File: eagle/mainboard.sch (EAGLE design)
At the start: 8 parts, among them Q1 TIP122, Q2 TIP122

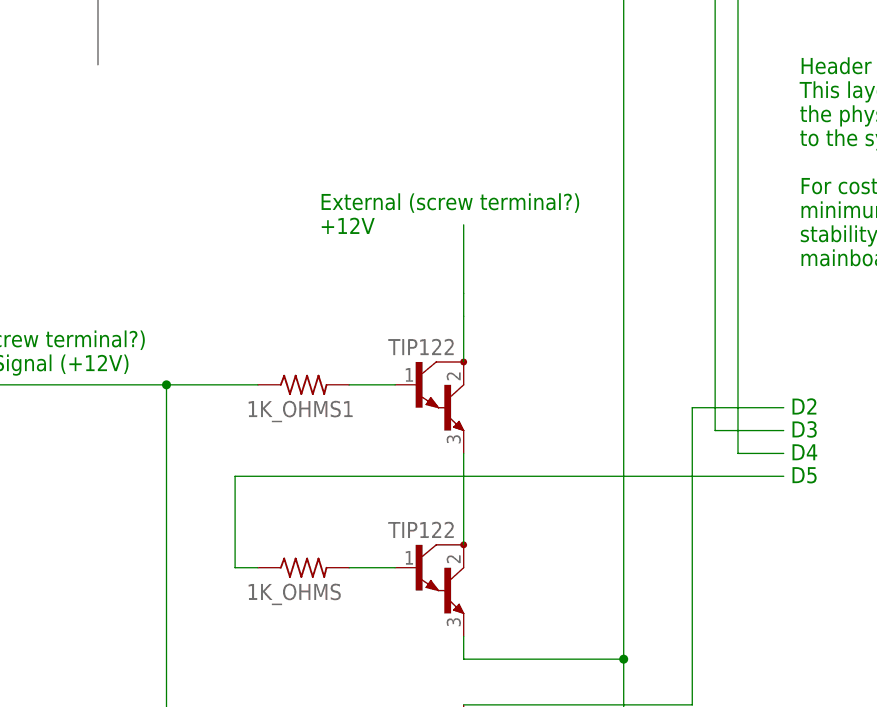
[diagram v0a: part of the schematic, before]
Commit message: 2.failed attempt to use the connection that the kill switch is breaking AS the SIGNAL to break the connection (yeah it didn't work)
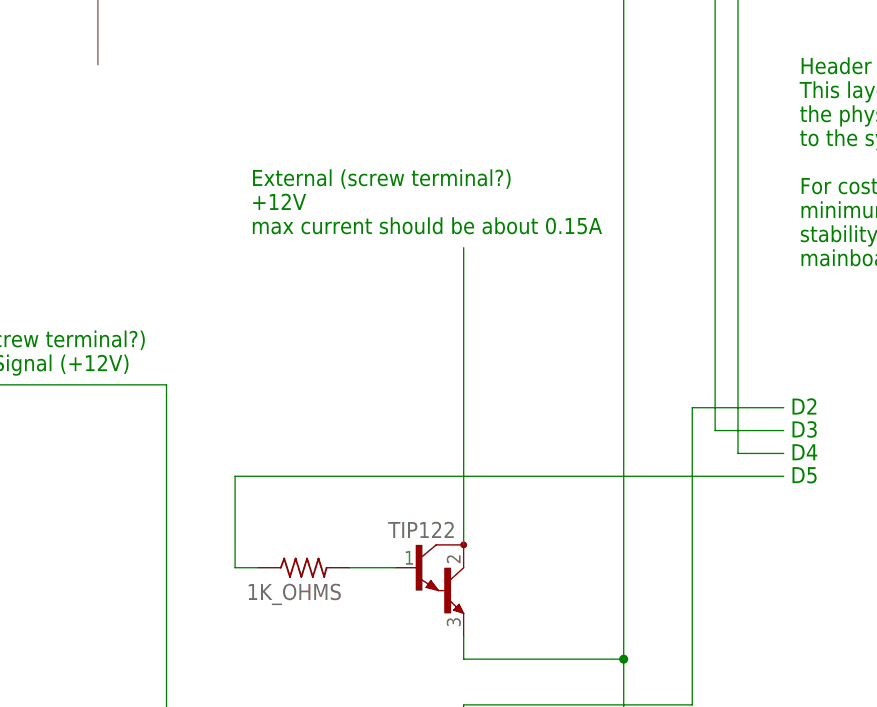
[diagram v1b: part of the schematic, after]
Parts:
- removed 1K_OHMS1: (no value), rcl:R-US_0411/15
- removed Q2: TIP122, transistor-npn:TIP122
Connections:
- removed net N$13: 1K_OHMS1.2, Q2.B
- removed net N$20: Q1.C, Q2.E
- removed net N$5: Q2.C
- new net N$3: Q1.C
- net N$21: no longer 1K_OHMS1.1
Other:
- note added: "External (screw terminal?) +12V max current should be about 0.15A"
- note removed: "External (screw terminal?) +12V"
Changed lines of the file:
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@@
 <part name="1K_OHMS" library="rcl" library_urn="urn:adsk.eagle:library:334" deviceset="R-US_" device="0411/15" package3d_urn="urn:adsk.eagle:package:23568/2"/>
 <part name="Q1" library="transistor-npn" library_urn="urn:adsk.eagle:library:398" deviceset="TIP122*" device="" package3d_urn="urn:adsk.eagle:package:28520/1"/>
-<part name="1K_OHMS1" library="rcl" library_urn="urn:adsk.eagle:library:334" deviceset="R-US_" device="0411/15" package3d_urn="urn:adsk.eagle:package:23568/2"/>
-<part name="Q2" library="transistor-npn" library_urn="urn:adsk.eagle:library:398" deviceset="TIP122*" device="" package3d_urn="urn:adsk.eagle:package:28520/1"/>
 <part name="D2" library="diode" library_urn="urn:adsk.eagle:library:210" deviceset="1N5400" device="" package3d_urn="urn:adsk.eagle:package:43365/2"/>
 <part name="10K_OHMS" library="rcl" library_urn="urn:adsk.eagle:library:334" deviceset="R-US_" device="0411/15" package3d_urn="urn:adsk.eagle:package:23568/2"/>
@@
 <sheet>
 <plain>
-<text x="4.318" y="26.924" size="1.778" layer="91">External (screw terminal?)
-+12V</text>
+<text x="-3.302" y="26.924" size="1.778" layer="91">External (screw terminal?)
++12V
+max current should be about 0.15A</text>
 <text x="-14.224" y="62.992" size="1.778" layer="91">External (screw terminal?)
 +5V</text>
@@
 <instance part="Q1" gate="G$1" x="15.24" y="-10.16" smashed="yes">
 <attribute name="VALUE" x="11.938" y="-6.858" size="1.778" layer="96"/>
-</instance>
-<instance part="1K_OHMS1" gate="G$1" x="2.54" y="10.16" smashed="yes">
-<attribute name="NAME" x="-3.81" y="6.5786" size="1.778" layer="95"/>
-<attribute name="VALUE" x="-1.27" y="6.858" size="1.778" layer="96"/>
-</instance>
-<instance part="Q2" gate="G$1" x="15.24" y="10.16" smashed="yes">
-<attribute name="VALUE" x="11.938" y="13.462" size="1.778" layer="96"/>
 </instance>
 <instance part="D2" gate="1" x="101.6" y="60.96" smashed="yes" rot="R270"/>
@@
 </segment>
 </net>
-<net name="N$5" class="0">
-<segment>
-<wire x1="20.32" y1="20.32" x2="20.32" y2="17.78" width="0.1524" layer="91"/>
-<pinref part="Q2" gate="G$1" pin="C"/>
-<wire x1="20.32" y1="17.78" x2="20.32" y2="12.7" width="0.1524" layer="91"/>
-<wire x1="20.32" y1="20.32" x2="20.32" y2="27.94" width="0.1524" layer="91"/>
-</segment>
-</net>
 <net name="N$6" class="0">
 <segment>
@@
 </segment>
 </net>
-<net name="N$13" class="0">
-<segment>
-<pinref part="1K_OHMS1" gate="G$1" pin="2"/>
-<pinref part="Q2" gate="G$1" pin="B"/>
-<wire x1="7.62" y1="10.16" x2="12.7" y2="10.16" width="0.1524" layer="91"/>
-</segment>
-</net>
-<net name="N$20" class="0">
-<segment>
-<pinref part="Q1" gate="G$1" pin="C"/>
-<wire x1="20.32" y1="2.54" x2="20.32" y2="-7.62" width="0.1524" layer="91"/>
-<pinref part="Q2" gate="G$1" pin="E"/>
-</segment>
-</net>
 <net name="N$21" class="0">
 <segment>
-<pinref part="1K_OHMS1" gate="G$1" pin="1"/>
-<wire x1="-2.54" y1="10.16" x2="-12.7" y2="10.16" width="0.1524" layer="91"/>
 <wire x1="-12.7" y1="10.16" x2="-33.02" y2="10.16" width="0.1524" layer="91"/>
 <wire x1="-12.7" y1="10.16" x2="-12.7" y2="-30.48" width="0.1524" layer="91"/>
-<junction x="-12.7" y="10.16"/>
 <pinref part="10K_OHMS" gate="G$1" pin="1"/>
 <wire x1="-12.7" y1="-30.48" x2="-2.54" y2="-30.48" width="0.1524" layer="91"/>
@@
 </segment>
 </net>
+<net name="N$3" class="0">
+<segment>
+<pinref part="Q1" gate="G$1" pin="C"/>
+<wire x1="20.32" y1="25.4" x2="20.32" y2="-7.62" width="0.1524" layer="91"/>
+</segment>
+</net>
